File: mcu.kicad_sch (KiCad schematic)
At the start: 11 parts

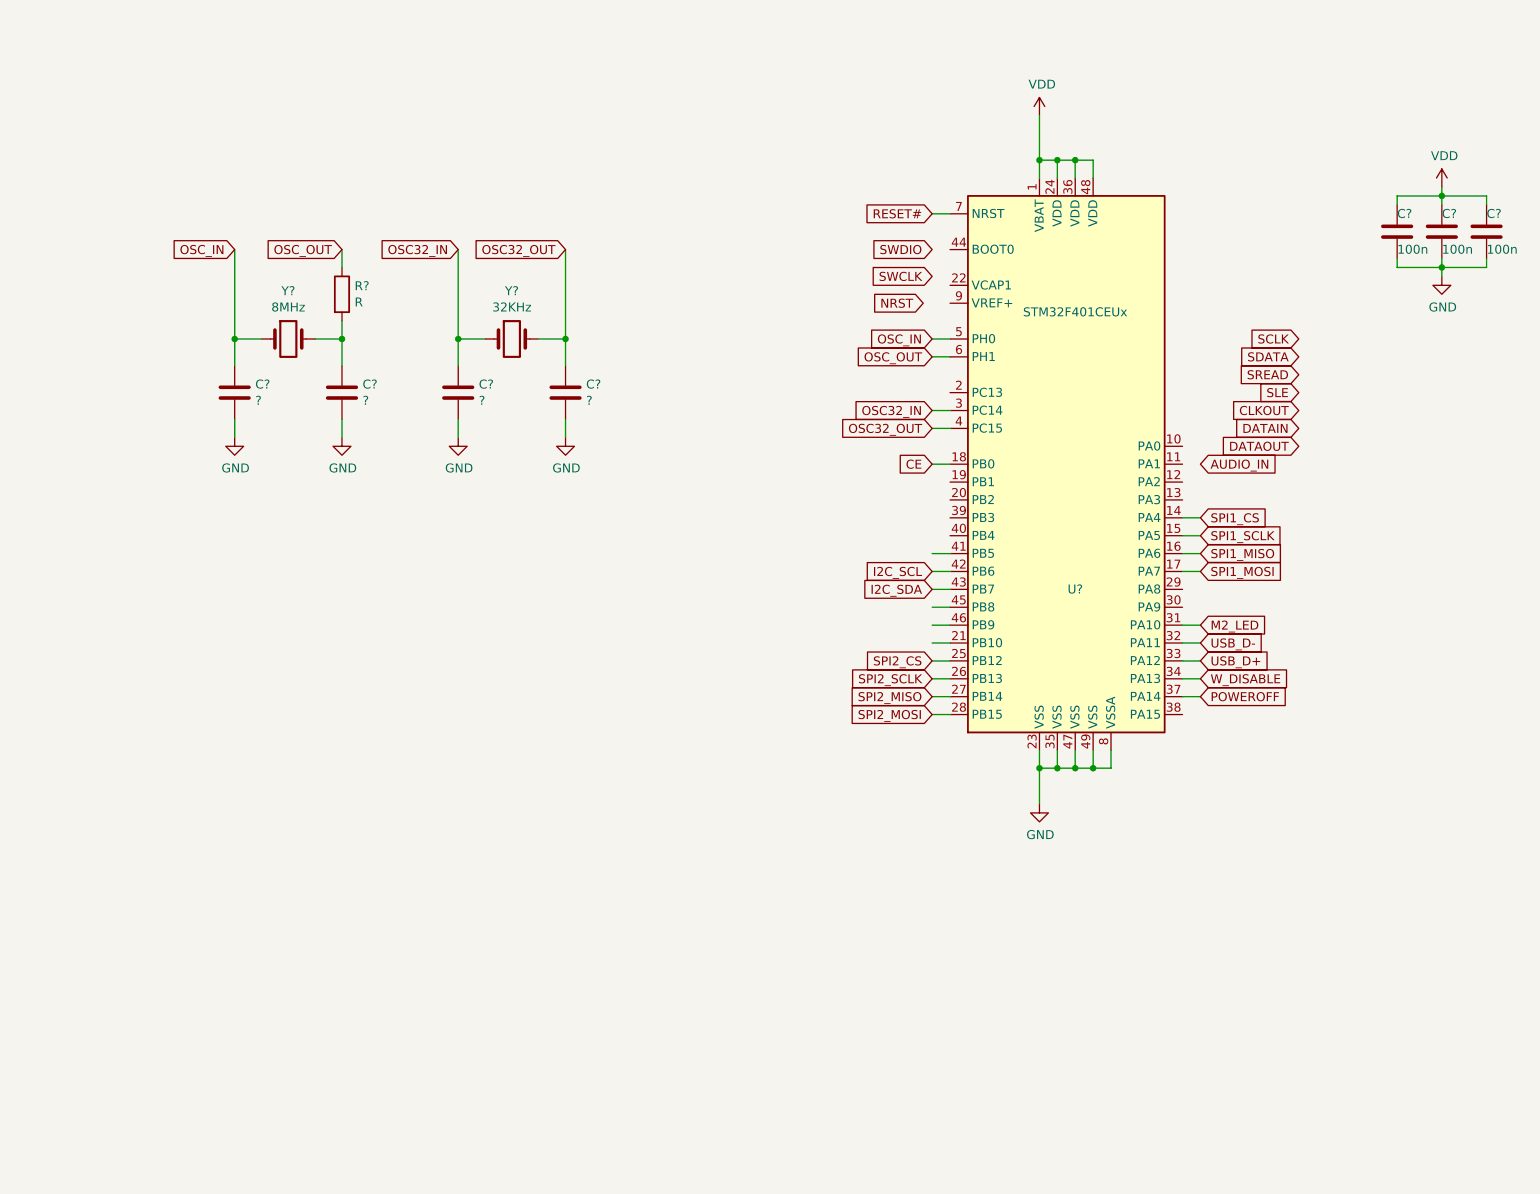
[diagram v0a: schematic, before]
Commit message: Replaced STM32 with ATSAMD51G
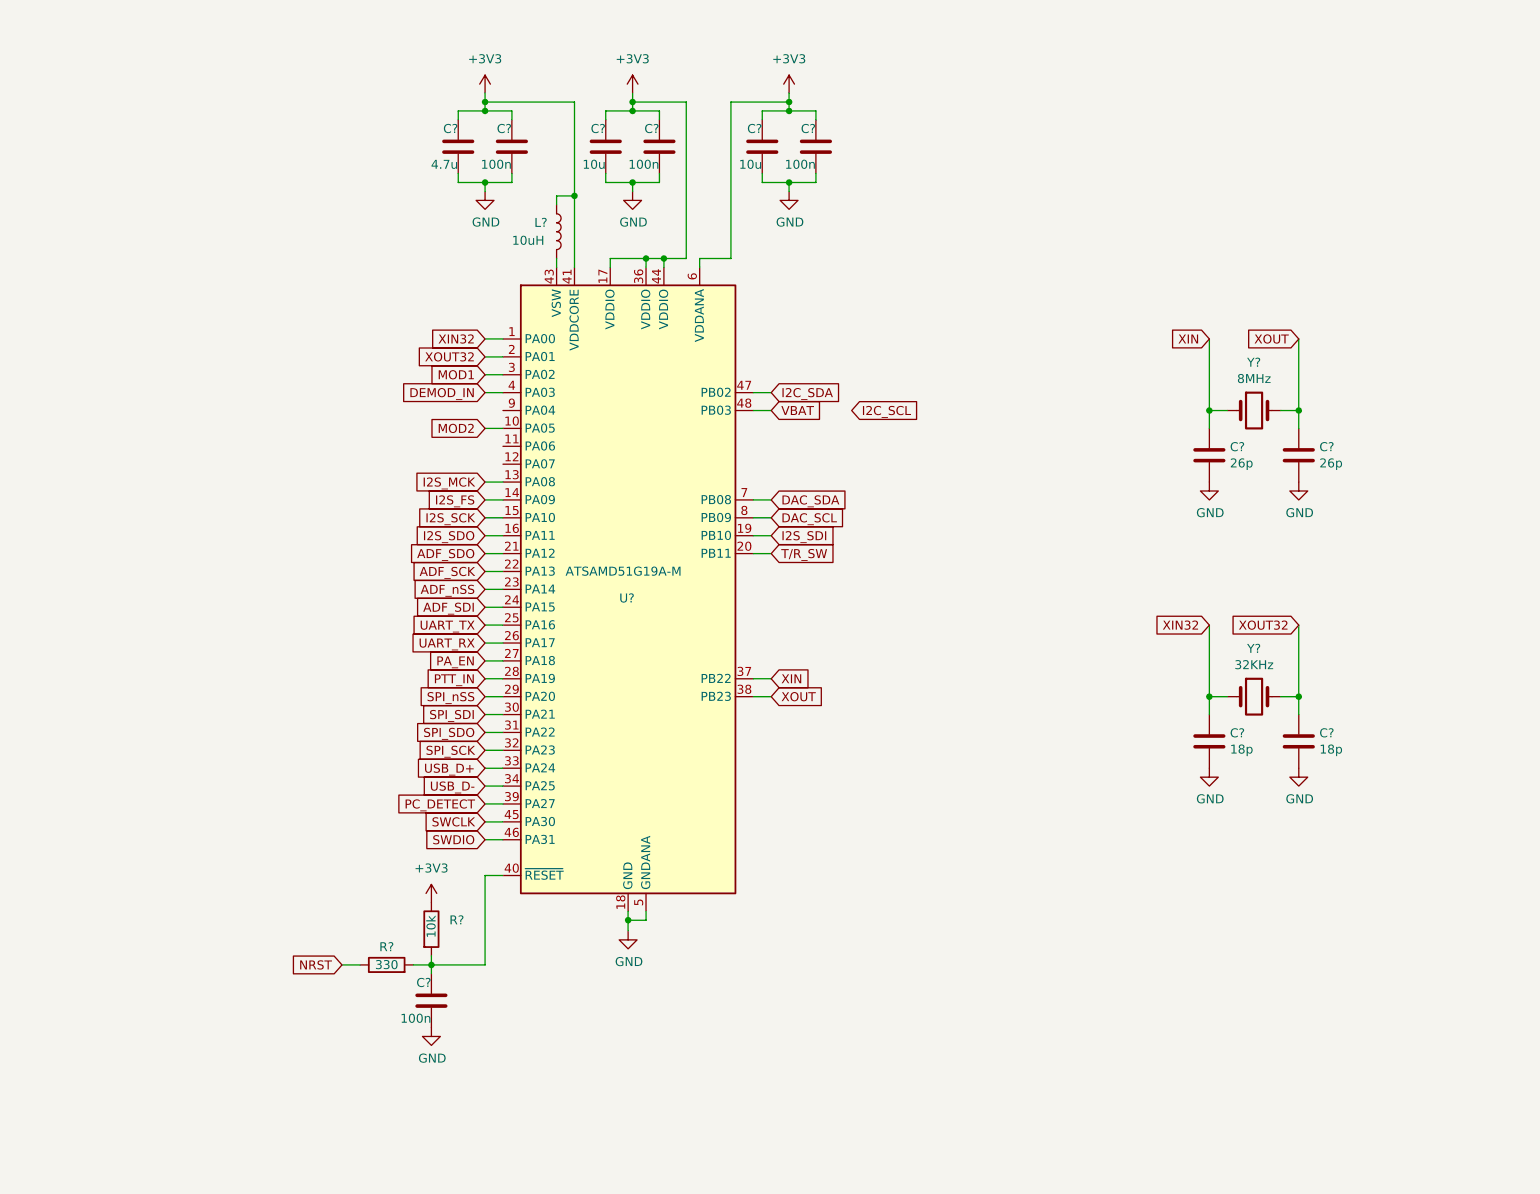
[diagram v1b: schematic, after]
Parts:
- removed C? (x2): ?, Capacitor_SMD:C_0402_1005Metric, symbol Device:C
- removed C? (x3): 100n, Capacitor_SMD:C_0402_1005Metric, symbol Device:C
- removed R?: R, Resistor_SMD:R_01005_0402Metric, symbol Device:R
- removed U?: STM32F401CEUx, Package_DFN_QFN:QFN-48-1EP_7x7mm_P0.5mm_EP5.6x5.6mm, symbol MCU_ST_STM32F4:STM32F401CEUx
- added C?: 4.7u, Capacitor_SMD:C_0402_1005Metric, symbol Device:C
- added C? (x4): 100n, Capacitor_SMD:C_0402_1005Metric, symbol Device:C
- added C? (x2): 26p, Capacitor_SMD:C_0402_1005Metric, symbol Device:C
- added C? (x2): 10u, Capacitor_SMD:C_0402_1005Metric, symbol Device:C
- added L?: 10uH, symbol Device:L
- added R?: 10k, symbol Device:R
- added R?: 330, symbol Device:R
- added U?: ATSAMD51G19A-M, Package_DFN_QFN:QFN-48-1EP_7x7mm_P0.5mm_EP5.15x5.15mm, symbol MCU_Microchip_ATSAMD51G:ATSAMD51G19A-M
- C? (x2): value ? -> 18p
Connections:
- net GND: now also C?.2, C?.2, C?.2, C?.2, C?.2, C?.2, C?.2, C?.2, C?.2, U?.18 (GND), U?.35 (GND), U?.42 (GND), U?.5 (GNDANA)
- net I2C_SDA: now also U?.47 (PB02)
- net NRST: now also R?.1
- net SWCLK: now also U?.45 (PA30)
- net SWDIO: now also U?.46 (PA31)
- net USB_D+: now also U?.33 (PA24)
- net USB_D-: now also U?.34 (PA25)
- net XOUT: now reaches Y?.2
- net XOUT: now also C?.1, U?.38 (PB23)
- net OSC32_IN renamed XIN32
- net XIN32: now also U?.1 (PA00)
- net OSC32_OUT renamed XOUT32
- net XOUT32: now also U?.2 (PA01)
- net OSC_IN renamed XIN
- net XIN: now also C?.1, U?.37 (PB22)
- new net: C?.1, R?.2, R?.2, U?.40 (~{RESET})
- new net: L?.2, U?.43 (VSW)
- new net +3V3: C?.1, C?.1, C?.1, C?.1, C?.1, C?.1, L?.1, R?.1, U?.17 (VDDIO), U?.36 (VDDIO), U?.41 (VDDCORE), U?.44 (VDDIO), U?.6 (VDDANA)
- new net ADF_SCK: U?.22 (PA13)
- new net ADF_SDI: U?.24 (PA15)
- new net ADF_SDO: U?.21 (PA12)
- new net ADF_nSS: U?.23 (PA14)
- new net DAC_SCL: U?.8 (PB09)
- new net DAC_SDA: U?.7 (PB08)
- new net DEMOD_IN: U?.4 (PA03)
- new net I2S_FS: U?.14 (PA09)
- new net I2S_MCK: U?.13 (PA08)
- new net I2S_SCK: U?.15 (PA10)
- new net I2S_SDI: U?.19 (PB10)
- new net I2S_SDO: U?.16 (PA11)
- new net MOD1: U?.3 (PA02)
- new net MOD2: U?.10 (PA05)
- new net PA_EN: U?.27 (PA18)
- new net PC_DETECT: U?.39 (PA27)
- new net PTT_IN: U?.28 (PA19)
- new net SPI_SCK: U?.32 (PA23)
- new net SPI_SDI: U?.30 (PA21)
- new net SPI_SDO: U?.31 (PA22)
- new net SPI_nSS: U?.29 (PA20)
- new net T/R_SW: U?.20 (PB11)
- new net UART_RX: U?.26 (PA17)
- new net UART_TX: U?.25 (PA16)
- new net VBAT: U?.48 (PB03)
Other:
- moved on the sheet: C?, Y?

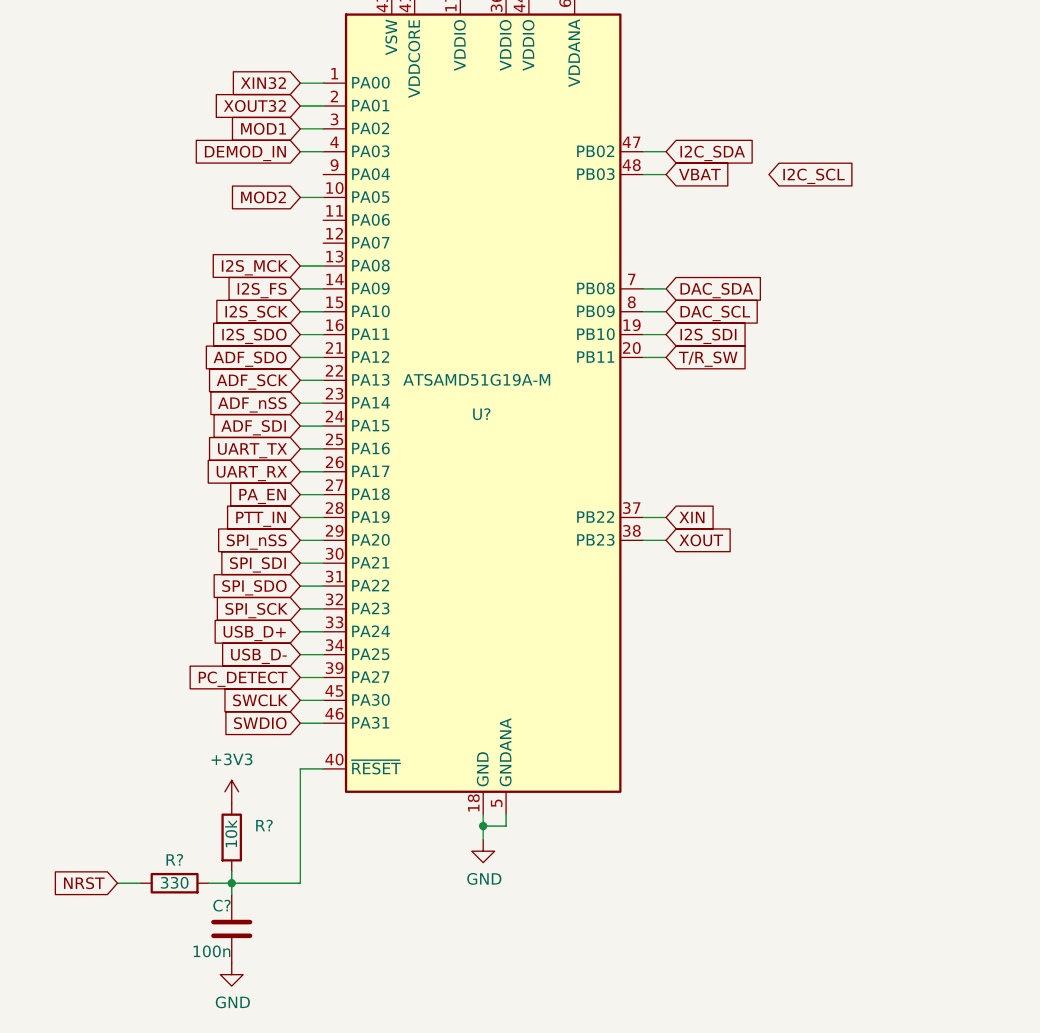
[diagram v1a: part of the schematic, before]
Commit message: Changed MCU and M.2 pin assignment
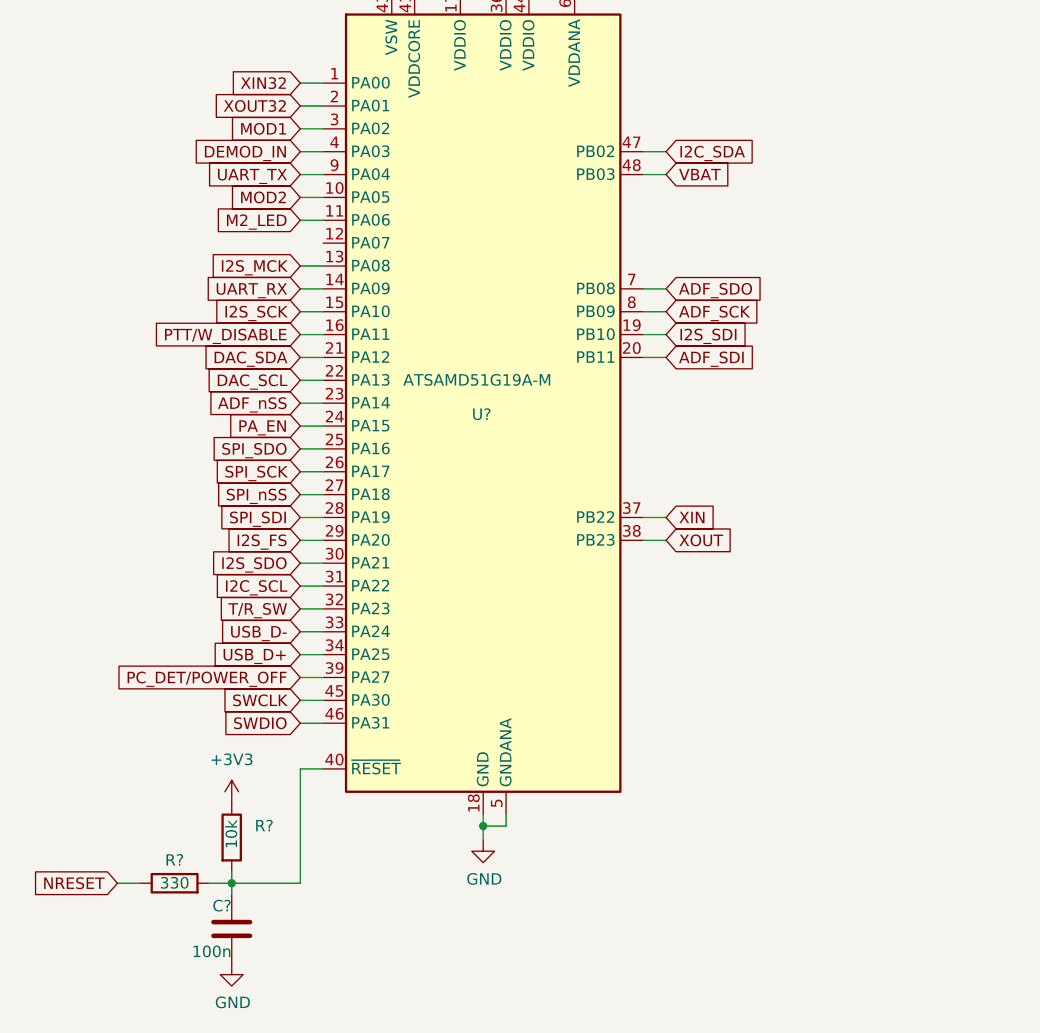
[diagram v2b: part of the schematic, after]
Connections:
- net PTT_IN is gone; now on net SPI_SDI: U?.28 (PA19)
- net ADF_SCK: now also U?.8 (PB09); no longer U?.22 (PA13)
- net ADF_SDI: now also U?.20 (PB11); no longer U?.24 (PA15)
- net ADF_SDO: now also U?.7 (PB08); no longer U?.21 (PA12)
- net DAC_SCL: now also U?.22 (PA13); no longer U?.8 (PB09)
- net DAC_SDA: now also U?.21 (PA12); no longer U?.7 (PB08)
- net I2C_SCL: now also U?.31 (PA22)
- net I2S_FS: now also U?.29 (PA20); no longer U?.14 (PA09)
- net I2S_SDO: now also U?.30 (PA21); no longer U?.16 (PA11)
- net PA_EN: now also U?.24 (PA15); no longer U?.27 (PA18)
- net SPI_SCK: now also U?.26 (PA17); no longer U?.32 (PA23)
- net SPI_SDI: no longer U?.30 (PA21)
- net SPI_SDO: now also U?.25 (PA16); no longer U?.31 (PA22)
- net SPI_nSS: now also U?.27 (PA18); no longer U?.29 (PA20)
- net T/R_SW: now also U?.32 (PA23); no longer U?.20 (PB11)
- net UART_RX: now also U?.14 (PA09); no longer U?.26 (PA17)
- net UART_TX: now also U?.9 (PA04); no longer U?.25 (PA16)
- net USB_D+: now also U?.34 (PA25); no longer U?.33 (PA24)
- net USB_D-: now also U?.33 (PA24); no longer U?.34 (PA25)
- net M2_LED: now reaches U?.11 (PA06)
- net NRST renamed NRESET
- net PC_DETECT renamed PC_DET/POWER_OFF
- new net PTT/W_DISABLE: U?.16 (PA11)
